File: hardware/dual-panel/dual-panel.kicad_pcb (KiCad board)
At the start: 4 copper layers, 139.7 x 127 mm, 151 parts, among them J1 USB_C_Receptacle_USB2.0_16P, J10 RS-485 OUT, J11 12V_OUT, J12 Conn_01x17, J13 Conn_01x17, J14 Conn_01x17, J15 Conn_01x17, J16 SWD, J3 FSR North, J4 FSR East, J5 12V_IN, J6 FSR South, J7 FSR West, J8 RS-485 IN, J9 INT OUT, SW1 PANEL_ID, SW2 BOOTSEL, SW3 RS-485 Termination, U1 RP2040, U2 THVD1429, U3 W25Q32JV, U4 SN74AHCT125, U5 AMS1117-5.0, U6 AP7361C-33ER-13, U7 USBLC6-2SC6, U8 LM66200, X1 12MHz ABM8-272-T3

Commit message: dual-panel: brain laid out, interface reworked to 4x 1x8, carrier routed
Work in progress checkpoint — not clean yet, see below.

Interface replaced: the two 1x17 rows became four 1x8 connectors, placed
in the two continuous free bands across the carrier (y~49-58 and y~83-92).
Carrier headers J12/J13/J14/J15 mate with brain sockets J2/J19/J17/J18;
both boards use the same relative layout, since the brain is translated
under the carrier rather than flipped. Grouped by function so the FSR
lines and the fast signals land on separate connectors.

Brain outline drawn at 76.1 x 63.6mm with its own GND_Brain pour, sitting
inside the measured 88 x 100mm frame opening with ~6mm per side in X.
Two M3 holes added per board (carrier H5/H6, brain H1/H2), registered to
the connectors; screw enters from the brain underside with a nut above
the carrier.

Cavity measured: 6mm from the carrier underside to the frame floor, plus
14mm to the cavity bottom, so 20mm of depth inside the opening. That
retires the depth gate and also means the carrier's four remaining
bottom-side parts (D30, R17, R20, C57, tallest 2.3mm) can stay put.

Known open, to fix next:
- +3.3VDC may be split into three islands with the regulator in only one
- +12VDC and VBUS each broken on the brain; VBUS leaves U8 unfed
- FSR_West does not land on R8 pad 1; J1 shell pad floating
- QSPI_SCLK clears GND_Brain by 0 in four places
- 180-degree rotation is only blocked by 0.50mm at the connectors; wants
  a 2.54mm Y delta between J15 and J14 for a half-pitch refusal
- screw scheme needs a board-to-board spacer, and the nuts land inside
  the LED field
- silkscreen deliberately untouched (110 of 115 DRC violations)

ERC 0, schematic parity 0. 25 unconnected, of which roughly 19 are the
expected cross-gap airwires at the mating connectors.
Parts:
- added H1: MountingHole_Pad, MountingHole:MountingHole_3.2mm_M3_Pad, F.Cu at (169.0, 78.0)
- added H2: MountingHole_Pad, MountingHole:MountingHole_3.2mm_M3_Pad, F.Cu at (217.3, 24.2)
- added H5: MountingHole_Pad, MountingHole:MountingHole_3.2mm_M3_Pad, F.Cu at (55.5, 97.5)
- added H6: MountingHole_Pad, MountingHole:MountingHole_3.2mm_M3_Pad, F.Cu at (103.8, 43.7)
- added J17: Conn_01x08_Socket, Connector_PinSocket_2.54mm:PinSocket_1x08_P2.54mm_Vertical, F.Cu at (176.2, 69.9)
- added J18: Conn_01x08_Socket, Connector_PinSocket_2.54mm:PinSocket_1x08_P2.54mm_Vertical, F.Cu at (222.7, 69.9)
- added J19: Conn_01x08_Socket, Connector_PinSocket_2.54mm:PinSocket_1x08_P2.54mm_Vertical, F.Cu at (222.7, 31.7)
- added J2: Conn_01x08_Socket, Connector_PinSocket_2.54mm:PinSocket_1x08_P2.54mm_Vertical, F.Cu at (176.2, 29.7)
- C1, C2, C3, C54, C56, C57, C8, R13, R14, R20: moved to F.Cu
- J12, J13, J14, J15: value Conn_01x17 -> Conn_01x08_Pin; footprint Connector_PinHeader_2.54mm:PinHeader_1x17_P2.54mm_Vertical -> Connector_PinHeader_2.54mm:PinHeader_1x08_P2.54mm_Vertical
- R2: moved to B.Cu
- moved J13 197.0 mm to (62.7, 89.4), turned to 90 degrees
- moved J15 192.7 mm to (62.7, 49.2), turned to 90 degrees
- moved J12 146.0 mm to (109.2, 89.4), turned to -90 degrees
- moved J14 143.6 mm to (109.2, 51.2), turned to -90 degrees
- moved TP15 138.1 mm to (128.7, 86.4)
- moved J1 115.4 mm to (167.3, 59.1), turned to -90 degrees
- moved R14 114.1 mm to (166.8, 69.4), turned to 0 degrees
- moved R13 111.4 mm to (166.5, 54.8), turned to 0 degrees
- moved J16 109.2 mm to (84.9, 55.7), turned to 90 degrees
- moved U7 106.8 mm to (171.0, 62.1), turned to 0 degrees
- moved D1 103.3 mm to (77.7, 56.7)
- moved R15 103.1 mm to (77.7, 54.4)
- moved R18 86.8 mm to (183.9, 37.6)
- moved C53 86.2 mm to (187.3, 37.7), turned to -90 degrees
- moved R19 86.1 mm to (185.6, 37.6), turned to -90 degrees
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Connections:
- J12 pad 3: FSR_East -> TERM_SENSE
- J12 pad 4: FSR_North -> GND
- J12 pad 5: FSR_West -> RS485+
- J12 pad 6: FSR_South -> RS485-
- J12 pad 8: INT_OUT -> FSR_East
- J13 pad 1: unconnected-(J13-Pin_1-Pad1) -> DIP_ID3
- J13 pad 2: unconnected-(J13-Pin_2-Pad2) -> DIP_ID2
- J13 pad 3: unconnected-(J13-Pin_3-Pad3) -> DIP_ID1
- J13 pad 4: unconnected-(J13-Pin_4-Pad4) -> DIP_ID0
- J13 pad 6: RS485- -> INT_OUT
- J13 pad 7: RS485+ -> GND
- J13 pad 8: GND -> FSR_South
- J14 pad 1: +3.3VDC -> +12VDC
- J14 pad 3: FSR_East -> GND
- J14 pad 4: FSR_North -> GND
- J14 pad 5: FSR_West -> LED_DATA_5V
- J14 pad 6: FSR_South -> GND
- J14 pad 7: GND -> SWCLK
- J14 pad 8: INT_OUT -> SWDIO
- J15 pad 1: unconnected-(J15-Pin_1-Pad1) -> +3.3VDC
- J15 pad 2: unconnected-(J15-Pin_2-Pad2) -> FSR_North
- J15 pad 3: unconnected-(J15-Pin_3-Pad3) -> FSR_West
- J15 pad 4: unconnected-(J15-Pin_4-Pad4) -> GND
- J15 pad 6: RS485- -> +12VDC
- J15 pad 7: RS485+ -> GND
- J15 pad 8: GND -> DEBUG_LED
- U1 pad 13: INT_OUT -> TERM_SENSE
- U1 pad 14: unconnected-(U1-GPIO11-Pad14) -> LED_DATA
- U1 pad 16: TERM_SENSE -> unconnected-(U1-GPIO13-Pad16)
- U1 pad 27: unconnected-(U1-GPIO16-Pad27) -> DEBUG_LED
- U1 pad 34: DEBUG_LED -> INT_OUT
- U1 pad 5: LED_DATA -> unconnected-(U1-GPIO3-Pad5)
- U1 pad 6: unconnected-(U1-GPIO4-Pad6) -> RS485_DE
- U1 pad 8: RS485_DE -> unconnected-(U1-GPIO6-Pad8)
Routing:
- net +3.3VDC: track 0.00 -> 411.1 mm, vias 0 -> 14
- net RS485+: track 0.00 -> 207.0 mm, vias 0 -> 1
- net RS485-: track 0.00 -> 206.0 mm, vias 0 -> 2
- net /carrier/RS485_Shield: track 0.00 -> 147.5 mm
- net TERM_SENSE: track 0.00 -> 102.0 mm, vias 0 -> 1
- net INT_OUT: track 0.00 -> 99.1 mm
- net FSR_South: track 0.00 -> 93.2 mm, vias 0 -> 1
- net LED_DATA_5V: track 45.0 -> 138.1 mm, vias 0 -> 1
- net FSR_West: track 0.00 -> 90.6 mm, vias 0 -> 1
- net FSR_East: track 0.00 -> 90.3 mm, vias 0 -> 1
- net FSR_North: track 0.00 -> 83.2 mm, vias 0 -> 1
- net GND: track 89.5 -> 169.4 mm, vias 260 -> 331
- net DIP_ID3: track 0.00 -> 64.5 mm
- net DIP_ID2: track 0.00 -> 62.2 mm
- net +5VDC: track 0.00 -> 60.7 mm, vias 0 -> 2
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- added copper zone on B.Cu, net GND
- added copper zone on F.Cu, net GND
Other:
- board size 139.7 x 127 mm -> 223.4 x 127 mm
- board text added: "FSR East"

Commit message: dual-panel: fully routed, DRC/ERC clean
Closes out the electrical fix list on hardware/dual-panel.

Routing / connectivity:
- +3.3VDC on the brain is one island again; the regulator (U6.2) now feeds
  RP2040 IOVDD and the ADC_AVDD branch instead of sitting isolated
- VBUS joined, so U8 (LM66200 power-OR) actually sees the USB rail
- FSR_West: landed C19 pad 1
- carrier +3.3VDC regions joined into a single rail
- fixed the GND connection-width neck at U8 pad 5 and a dangling VBUS via
- snapped J19 back onto the shared interface grid (222.693629)

Interface:
- carrier headers J12-J15 flipped to B.Cu so they point down at the brain;
  sockets J17/J18/J19/J2 stay on the brain's top side
- mate map re-verified pad-for-pad and net-for-net at offset
  (113.493629, -19.47): J15<->J2, J14<->J19, J13<->J17, J12<->J18
- 180-degree rotation offset widened to 2.00mm (1.00mm mismatch)

Silkscreen:
- cleared all 108 violations, including four stray F.SilkS alignment guides
  that ran between the connector pin-1s

Verified: DRC 0 violations, ERC 0, 19 unconnected - all of them the expected
cross-gap airwires between mating connectors, one per crossing net. Stable
across a fresh zone refill. The 92 schematic-parity net_conflicts are a
pre-existing cosmetic naming artifact (PWR_FLAG-derived names), not topology.
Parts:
- J12, J13, J14, J15: moved to B.Cu
- turned J12 to 90 degrees
- turned J13 to -90 degrees
- turned J14 to 90 degrees
- turned J15 to -90 degrees
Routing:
- net +3.3VDC: track 411.1 -> 517.2 mm, vias 14 -> 16
- net VBUS: track 30.0 -> 132.5 mm, vias 1 -> 2
- net +12VDC: track 907.4 -> 945.1 mm
- net GND: track 169.4 -> 167.0 mm, vias 331 -> 330
- net FSR_West: track 90.6 -> 91.6 mm

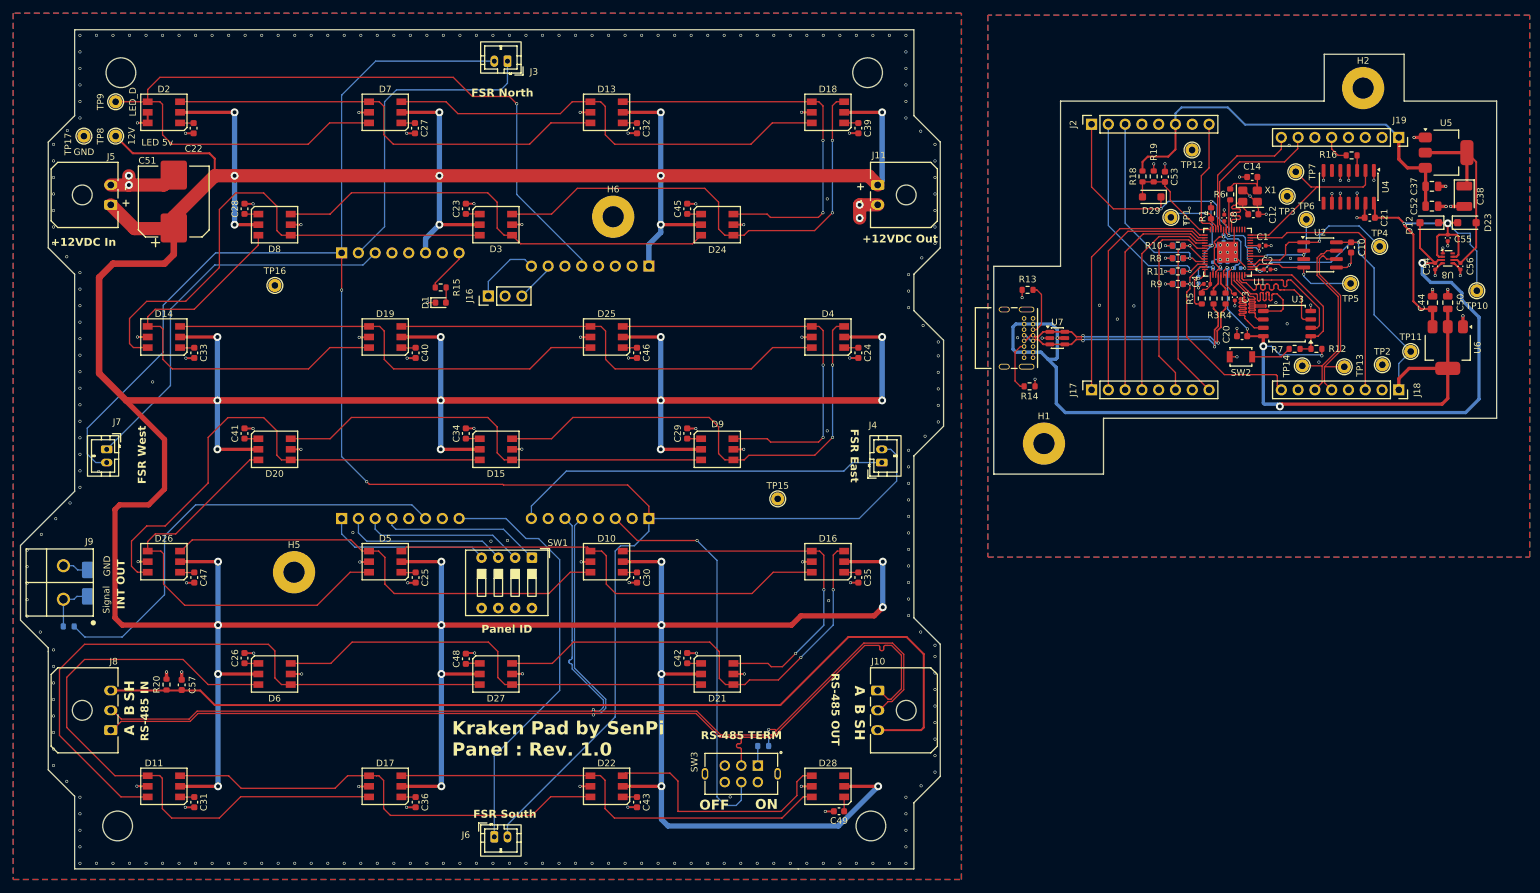
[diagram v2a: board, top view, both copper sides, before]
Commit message: dual-panel: USB to south edge, reshaped outlines, measured mechanical stack
Board:
- J1 moved from the west edge to the brain's south edge. Its body overhung the
  west outline by 3.20mm, leaving 2.94mm to the cavity wall where the outline
  alone suggested 6.11mm; it now has 24.70mm. The south edge was not free
  (J17/J18 and SW2), so the brain was extended south to make room.
- chamfers and fillets on both outlines; west lobe trimmed back now that only
  H1 holds that edge out
- H1 and H5 both moved by (+2.5, -2.0), preserving registration exactly

Verified: DRC 0, ERC 0, 19 unconnected and all of them cross-gap, silk still 0
despite the new chamfers. Registration offset (113.493629, -19.47) agrees across
all six mating pairs, and the mate map matches pad-for-pad on all 32 pins.

Docs - the cavity gate is CLOSED. The printed fit test confirmed the 88x100
opening is centred on the mounting-hole pattern, so the window is measured, not
assumed. README gains a Mechanical stack section with caliper measurements:
10.75mm board-to-board, 15.35mm total under the carrier of 20mm available, an
11mm M3 spacer erring tall, and the header pin-length constraint that makes the
stack behave (the 8mm-mating headers on hand bottom out in an 8.30mm socket).
Open gates trimmed to the three that are actually still open.
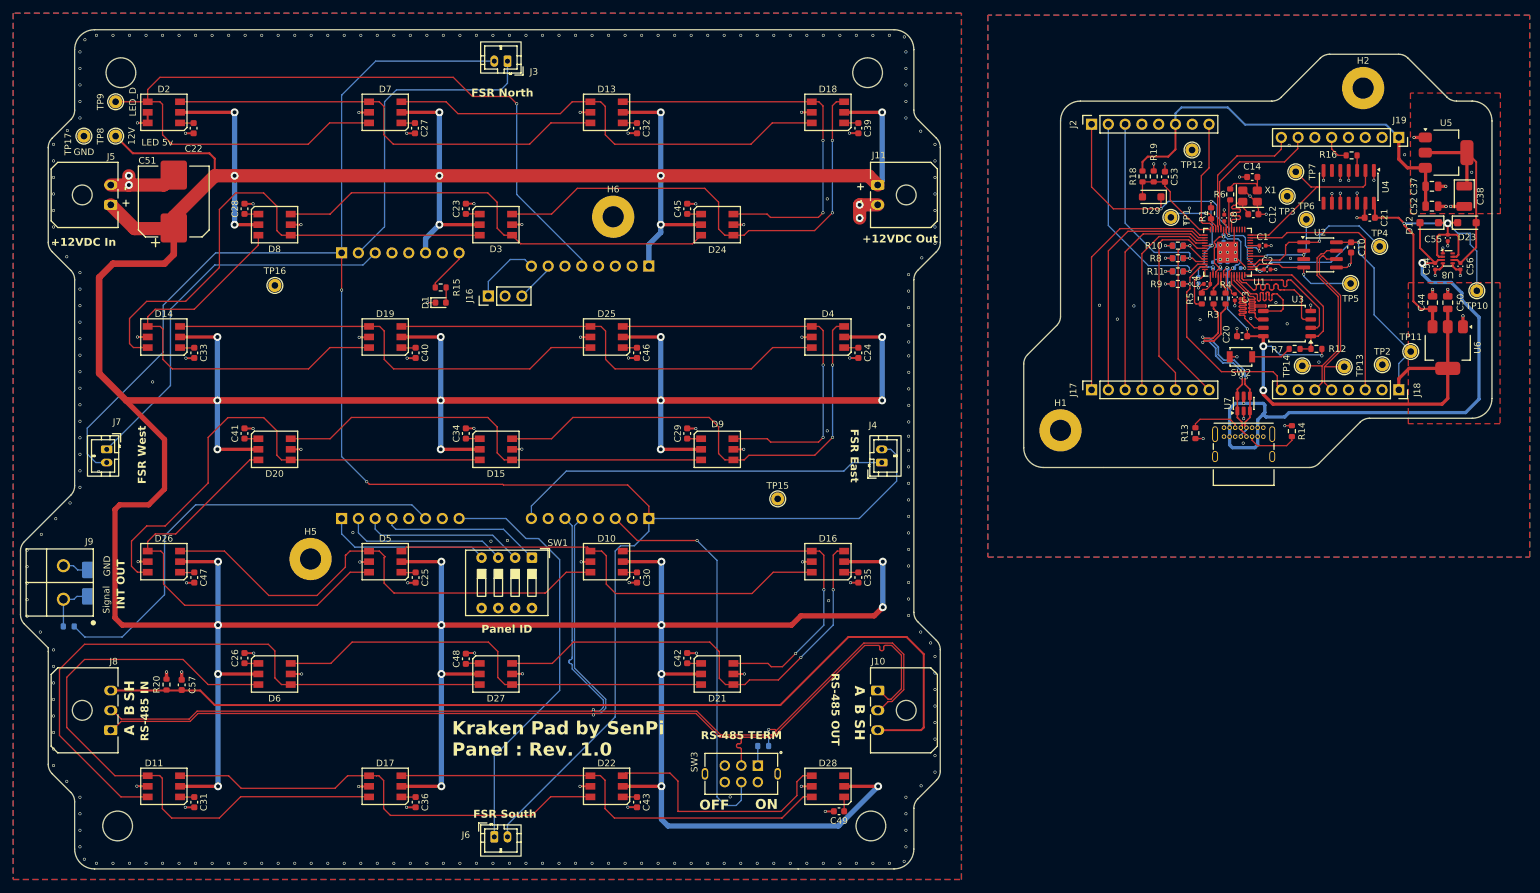
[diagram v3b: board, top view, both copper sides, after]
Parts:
- moved R14 40.3 mm to (206.5, 76.2), turned to 90 degrees
- moved R13 33.4 mm to (191.9, 76.5), turned to 90 degrees
- moved J1 33.3 mm to (196.2, 75.6), turned to 0 degrees
- moved U7 29.9 mm to (199.2, 72.0), turned to 90 degrees
- moved H1 3.20 mm to (171.5, 76.0)
- moved H5 3.20 mm to (58.0, 95.5)
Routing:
- net VBUS: track 132.5 -> 93.8 mm
- net USB_D-: track 37.7 -> 27.8 mm
- net USB_D+: track 37.5 -> 27.8 mm
- net /carrier/LD15: track 69.9 -> 75.2 mm
- net +3.3VDC: track 517.2 -> 516.2 mm
- net GND: track 167.0 -> 167.6 mm, vias 330 -> 334
- added copper zone on F.Cu, net +3.3VDC
- added copper zone on F.Cu, net /brain/+5VDC_AMS
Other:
- board size 223.4 x 127 mm -> 222.7 x 127 mm

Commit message: dual-panel: carrier test points + brain labelling
Carrier test points, 5 -> 18. The brain is buried under the carrier, so its
test points need the stack apart; these are the ones reachable on a working pad.

- reachable-only-here: TP18/TP19 RS485+/-, TP20 +3.3VDC (the FSR excitation
  rail, which had no carrier test point at all), TP21 on the INT terminal side
  of R17
- LED chain bisect: TP22/TP23/TP24/TP25 on LD6, LD12, LD18, LD23, so a dead
  chain localises in a couple of probes instead of hunting 25 parts
- TP26 +12VDC at the far end of the spine, to measure real IR drop across the
  LED field against the ~18mV the comb topology was chosen on
- TP27 TERM_SENSE, and TP28/TP29/TP30 GND so each probe cluster has a local
  return

Deliberately left off: the four FSR lines (highest-impedance nets on the board,
dividers are on the brain so the carrier side is raw sensor line, and the
isolation from LED data was deliberate - probe the JST-PH connectors instead)
and DIP_ID0-3 (probe SW1 directly).

Also silkscreen labelling on the brain.

Verified: DRC 0, ERC 0, 19 unconnected and all cross-gap. Test points are
synced 30/30 between schematic and PCB with matching UUID links. Parity is 93,
up one only because TP21 joined Net-(D30-K), a net already in the pre-existing
cosmetic naming class.
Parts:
- added TP18: GND, TestPoint:TestPoint_THTPad_D2.0mm_Drill1.0mm, F.Cu at (35.8, 122.1)
- added TP19: GND, TestPoint:TestPoint_THTPad_D2.0mm_Drill1.0mm, F.Cu at (35.8, 117.7)
- added TP20: GND, TestPoint:TestPoint_THTPad_D2.0mm_Drill1.0mm, F.Cu at (118.5, 138.4)
- added TP21: GND, TestPoint:TestPoint_THTPad_D2.0mm_Drill1.0mm, F.Cu at (21.6, 91.5)
- added TP22: GND, TestPoint:TestPoint_THTPad_D2.0mm_Drill1.0mm, F.Cu at (66.1, 43.0)
- added TP23: GND, TestPoint:TestPoint_THTPad_D2.0mm_Drill1.0mm, F.Cu at (118.4, 86.4)
- added TP24: GND, TestPoint:TestPoint_THTPad_D2.0mm_Drill1.0mm, F.Cu at (129.2, 86.4)
- added TP25: GND, TestPoint:TestPoint_THTPad_D2.0mm_Drill1.0mm, F.Cu at (133.1, 138.4)
- added TP26: +12VDC, TestPoint:TestPoint_THTPad_D2.0mm_Drill1.0mm, F.Cu at (137.8, 138.4)
- added TP27: +12VDC, TestPoint:TestPoint_THTPad_D2.0mm_Drill1.0mm, F.Cu at (123.2, 138.4)
- added TP28: GND, TestPoint:TestPoint_THTPad_D2.0mm_Drill1.0mm, F.Cu at (25.4, 87.5)
- added TP29: GND, TestPoint:TestPoint_THTPad_D2.0mm_Drill1.0mm, F.Cu at (41.0, 124.9)
- added TP30: GND, TestPoint:TestPoint_THTPad_D2.0mm_Drill1.0mm, F.Cu at (128.1, 138.4)
- moved TP16 23.1 mm to (72.9, 43.1)
- moved TP15 4.89 mm to (123.8, 86.4)
- moved TP12 4.54 mm to (191.0, 38.1)
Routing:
- net +3.3VDC: track 516.2 -> 547.3 mm
- net TERM_SENSE: track 102.0 -> 121.7 mm, vias 1 -> 2
- net /carrier/LD18: track 71.2 -> 88.1 mm
- net Net-(D30-K): track 8.00 -> 20.6 mm
- net /carrier/LD6: track 77.6 -> 90.2 mm
- net /carrier/LD23: track 68.6 -> 75.8 mm
- net /carrier/LD12: track 68.4 -> 74.8 mm
- net +12VDC: track 945.1 -> 947.7 mm
- net RS485-: track 206.0 -> 208.0 mm
- net RS485+: track 207.0 -> 209.0 mm
- net GND: vias 334 -> 374
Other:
- board text added: "+12V"
- board text added: "+3.3V"
- board text added: "+5V"
- board text added: "485+"
- board text added: "485-"
- board text added: "DE"
- board text added: "INT"
- board text added: "Kraken Pad by SenPi Brain : Rev. 1.0"
- board text added: "Kraken Pad by SenPi Carrier : Rev. 1.0"
- board text added: "LD12"
- board text added: "LD18"
- board text added: "LD23"
- board text added: "LD6"
- board text added: "LED"
- board text added: "RS485+"
- board text added: "RS485-"
- board text added: "RUN"
- board text added: "RX"
- board text added: "TERM"
- board text added: "TX"
- board text removed: "12V"
- board text removed: "Kraken Pad by SenPi Panel : Rev. 1.0"
